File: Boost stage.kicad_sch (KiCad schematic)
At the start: 1 part, among them U49 INA2227AIYBJR

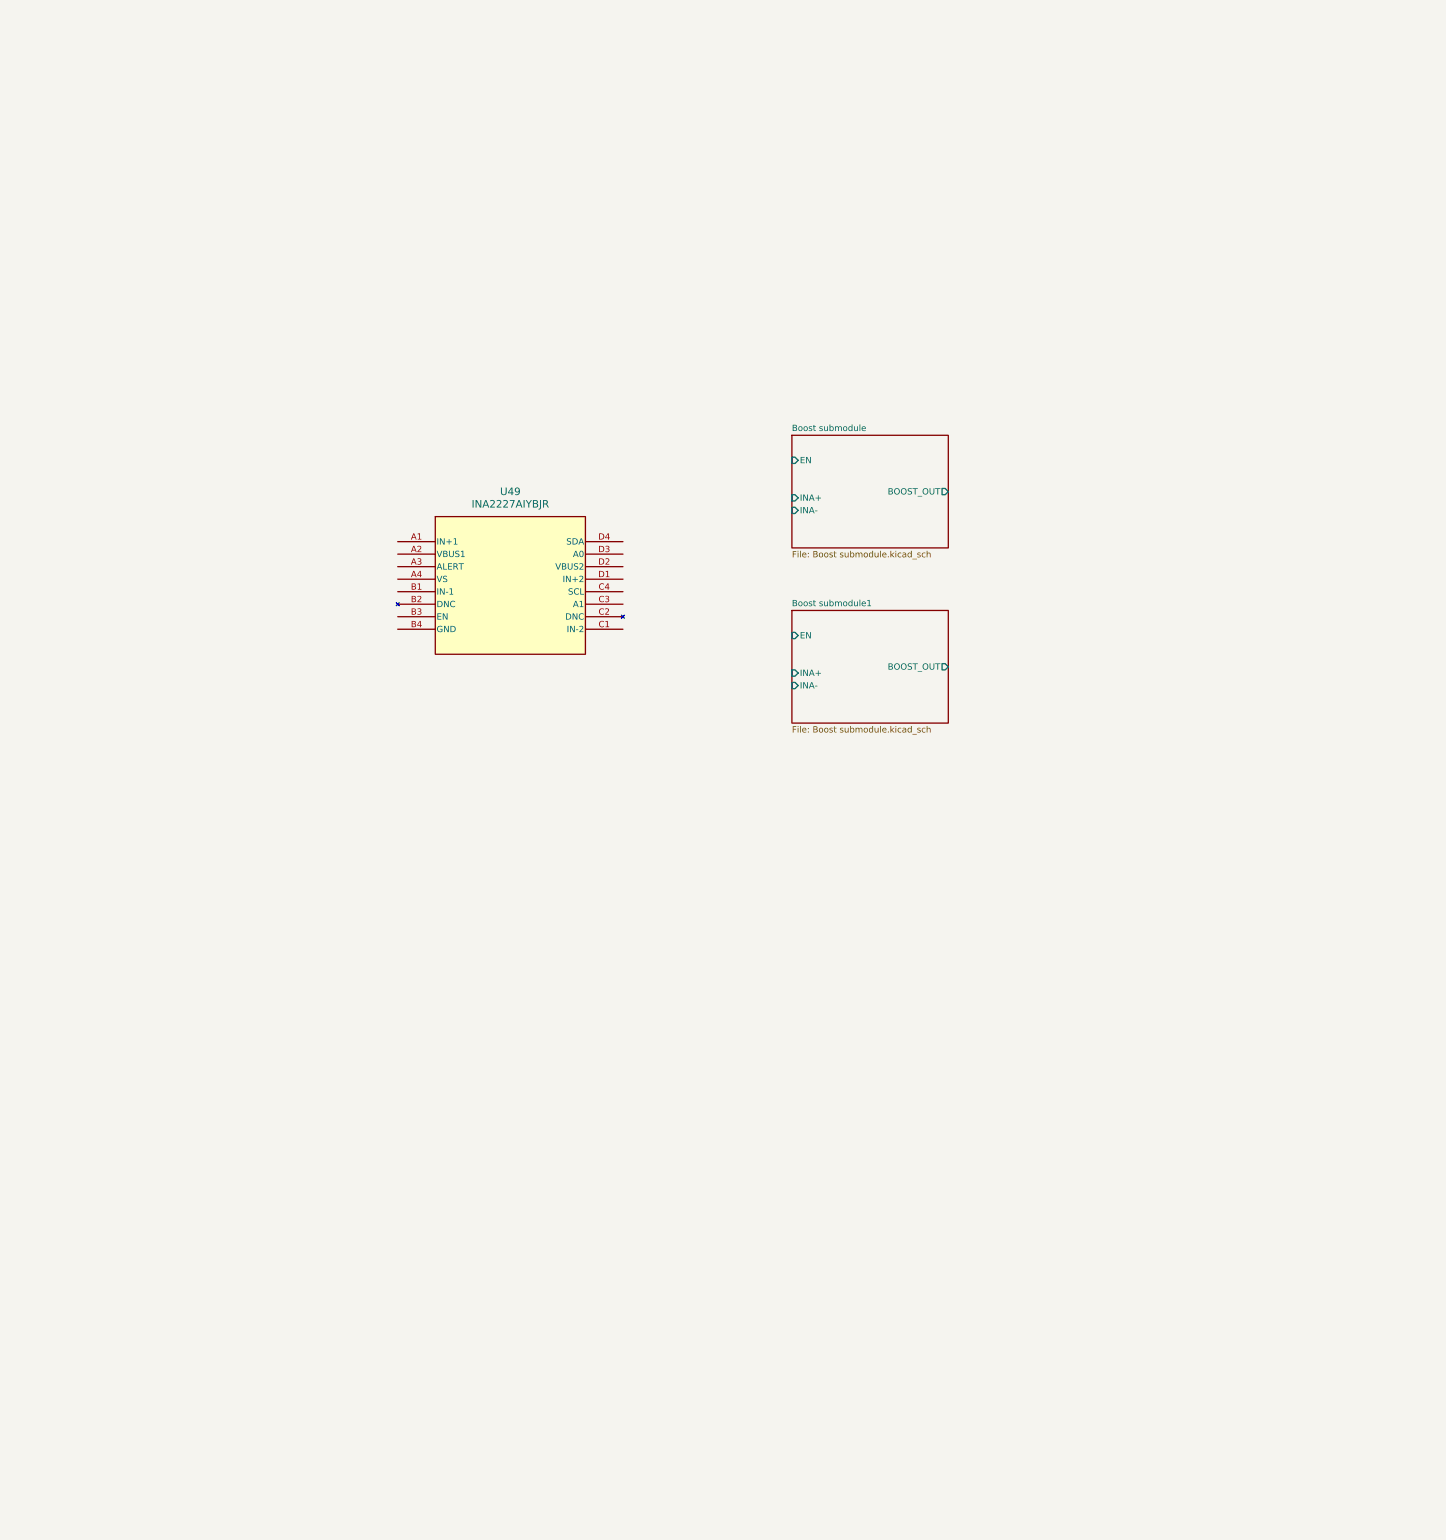
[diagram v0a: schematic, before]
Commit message: HW-61 chore: FT4233 Wire'd up
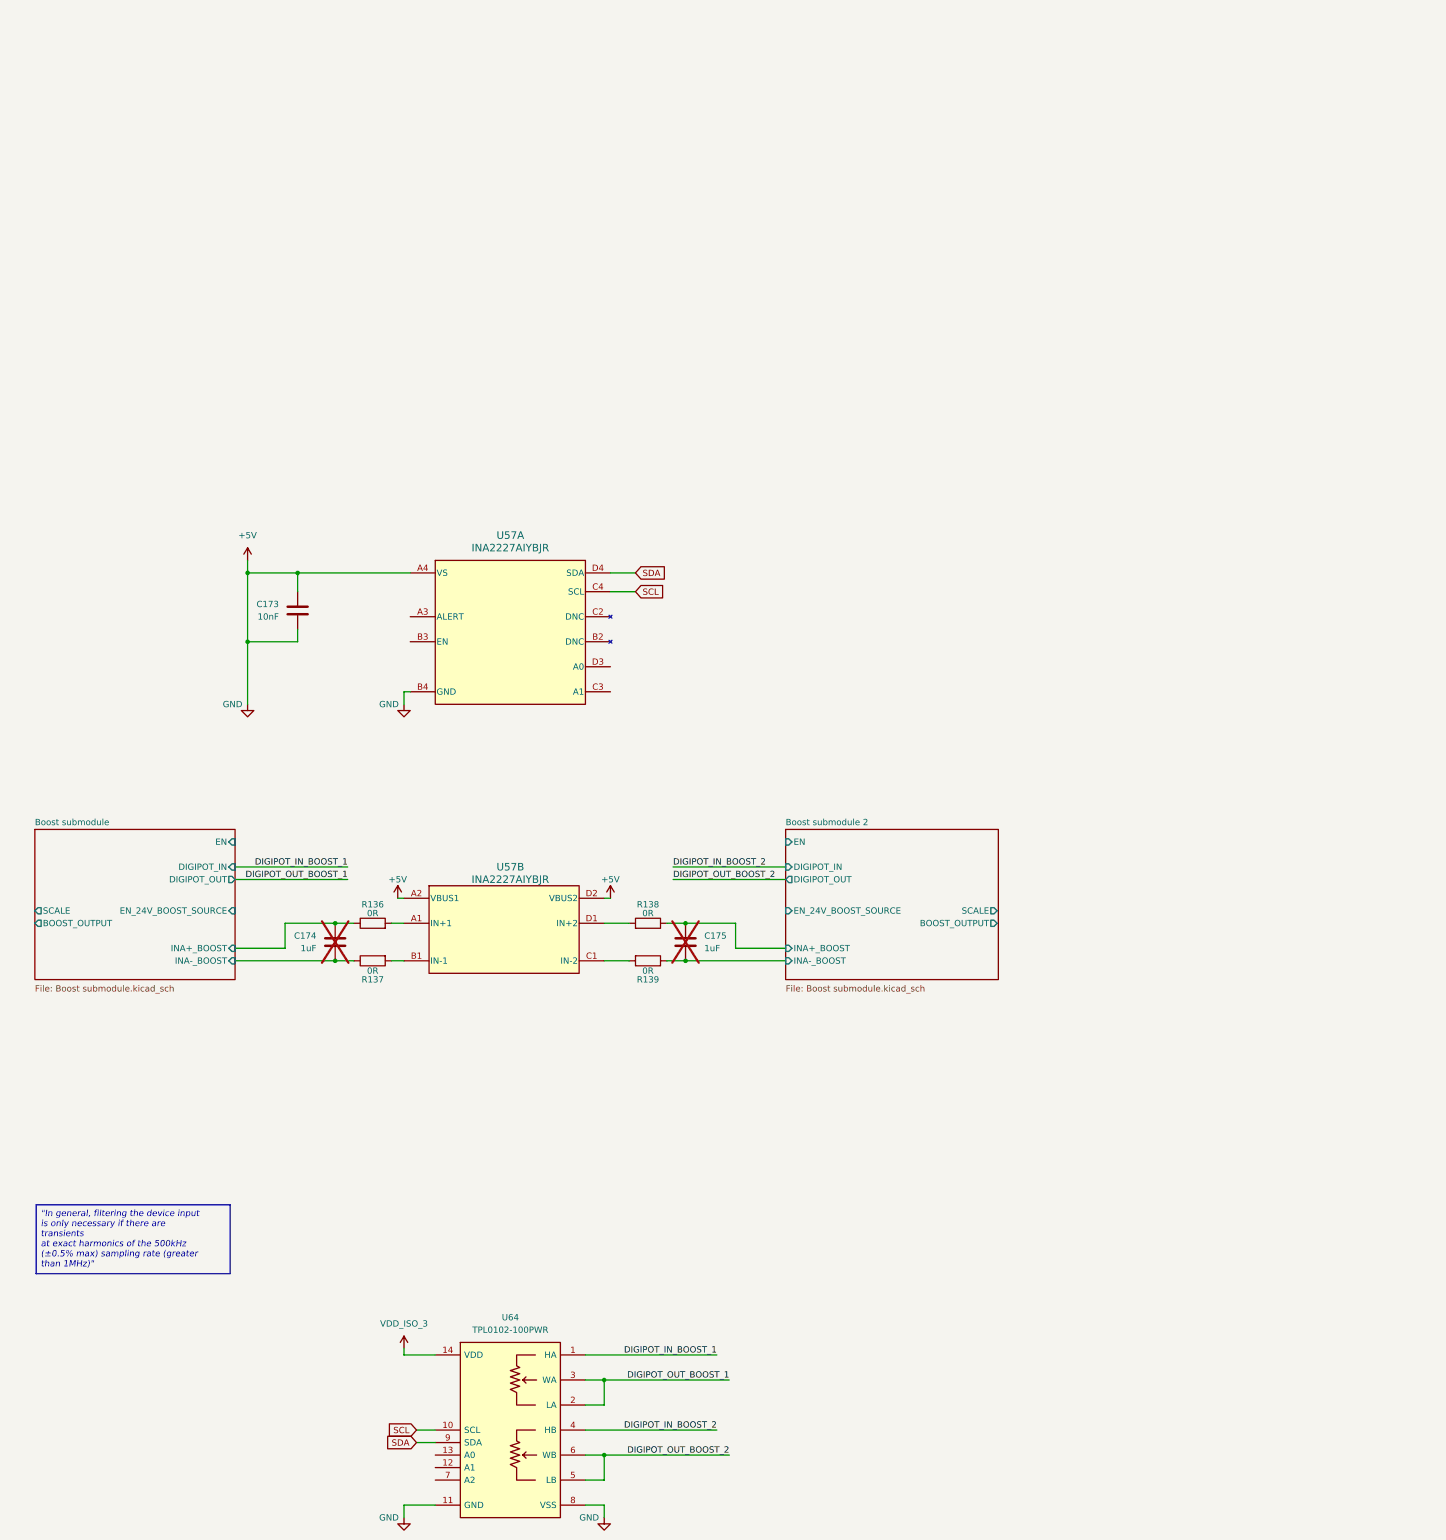
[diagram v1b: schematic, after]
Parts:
- removed U49: INA2227AIYBJR, digikey:U_BGA_YBJ0016-C01_TEX-M, symbol digikey:INA2227AIYBJR
- added C173: 10nF-0402_01, passive:Capacitor_0402, symbol capacitor:10nF-0402_01
- added C174, C175: 1uF-0402_01, passive:Capacitor_0402, symbol capacitor:1uF-0402_01
- added R136, R137, R138, R139: 0R-0402_01, passive:Resistor_0402, symbol resistor:0R-0402_01
- added U57: INA2227AIYBJR, review:DSBGA-16_P0.4_1.508X1.508mm, symbol staging:INA2227AIYBJR
- added U64: TPL0102-100PWR, semiconductor:TSSOP-14_P0.65_4.4x5x1.2, symbol integrated-circuit:TPL0102-100PWR
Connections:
- new net: R139.2, U57.C1 (IN-2)
- new net: R136.2, U57.A1 (IN+1)
- new net: R137.2, U57.B1 (IN-1)
- new net: R138.2, U57.D1 (IN+2)
- new net +5V: C173.1, C173.2, U57.A2 (VBUS1), U57.A4 (VS), U57.B4 (GND), U57.D2 (VBUS2), U64.11 (GND), U64.8 (VSS)
- new net Boost submodule 2/INA+_BOOST: C175.1, R138.1
- new net Boost submodule 2/INA-_BOOST: C175.2, R139.1
- new net Boost submodule/INA+_BOOST: C174.1, R136.1
- new net Boost submodule/INA-_BOOST: C174.2, R137.1
- new net DIGIPOT_IN_BOOST_1: U64.1 (HA)
- new net DIGIPOT_IN_BOOST_2: U64.4 (HB)
- new net DIGIPOT_OUT_BOOST_1: U64.2 (LA), U64.3 (WA)
- new net DIGIPOT_OUT_BOOST_2: U64.5 (LB), U64.6 (WB)
- new net SCL: U57.C4 (SCL), U64.10 (SCL)
- new net SDA: U57.D4 (SDA), U64.9 (SDA)
- new net VDD_ISO_3: U64.14 (VDD)
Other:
- removed sheet Boost submodule1
- added sheet Boost submodule 2 (Boost submodule.kicad_sch)
- sheet Boost submodule ports: added BOOST_OUTPUT, DIGIPOT_IN, DIGIPOT_OUT, EN_24V_BOOST_SOURCE, INA+_BOOST, INA-_BOOST, SCALE; removed BOOST_OUT, INA+, INA-

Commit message: Details to finish
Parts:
- added U68: PCA9535PWR, semiconductor:TSSOP-24_P0.65_7.8x4.4x1.2, symbol integrated-circuit:PCA9535PWR
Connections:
- net +5V: now also U57.B3 (EN), U57.D3 (A0), U68.12 (GND), U68.24 (VDD)
- net SCL: now also U68.22 (SCL)
- net SDA: now also U57.C3 (A1), U68.23 (SDA)
- net Boost submodule 2/INA+_BOOST renamed +INA_BOOST_2
- net Boost submodule 2/INA-_BOOST renamed -INA_BOOST_2
- net Boost submodule/INA+_BOOST renamed +INA_BOOST_1
- net Boost submodule/INA-_BOOST renamed -INA_BOOST_1
- new net EN_BOOST_1: U68.4 (P00_B)
- new net EN_BOOST_2: U68.7 (P03_B)
- new net FEED_24V_BOOST_1: U68.6 (P02_B)
- new net FEED_24V_BOOST_2: U68.9 (P05_B)
- new net FEED_5V_BOOST_1: U68.5 (P01_B)
- new net FEED_5V_BOOST_2: U68.8 (P04_B)
- new net SCALE_BOOST_1: U68.10 (P06_B)
- new net SCALE_BOOST_2: U68.11 (P07_B)
- no-connect marks 0 -> 2
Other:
- sheet Boost submodule ports: added EN_5V_BOOST_SOURCE, EN_BOOST; removed EN
- sheet Boost submodule 2 ports: added EN_5V_BOOST_SOURCE, EN_BOOST; removed EN
- note added: "I2C ID: 0x49"
- moved on the sheet: C173, C174, C175, R136, R137, R138, R139, U57A, U57B, U64

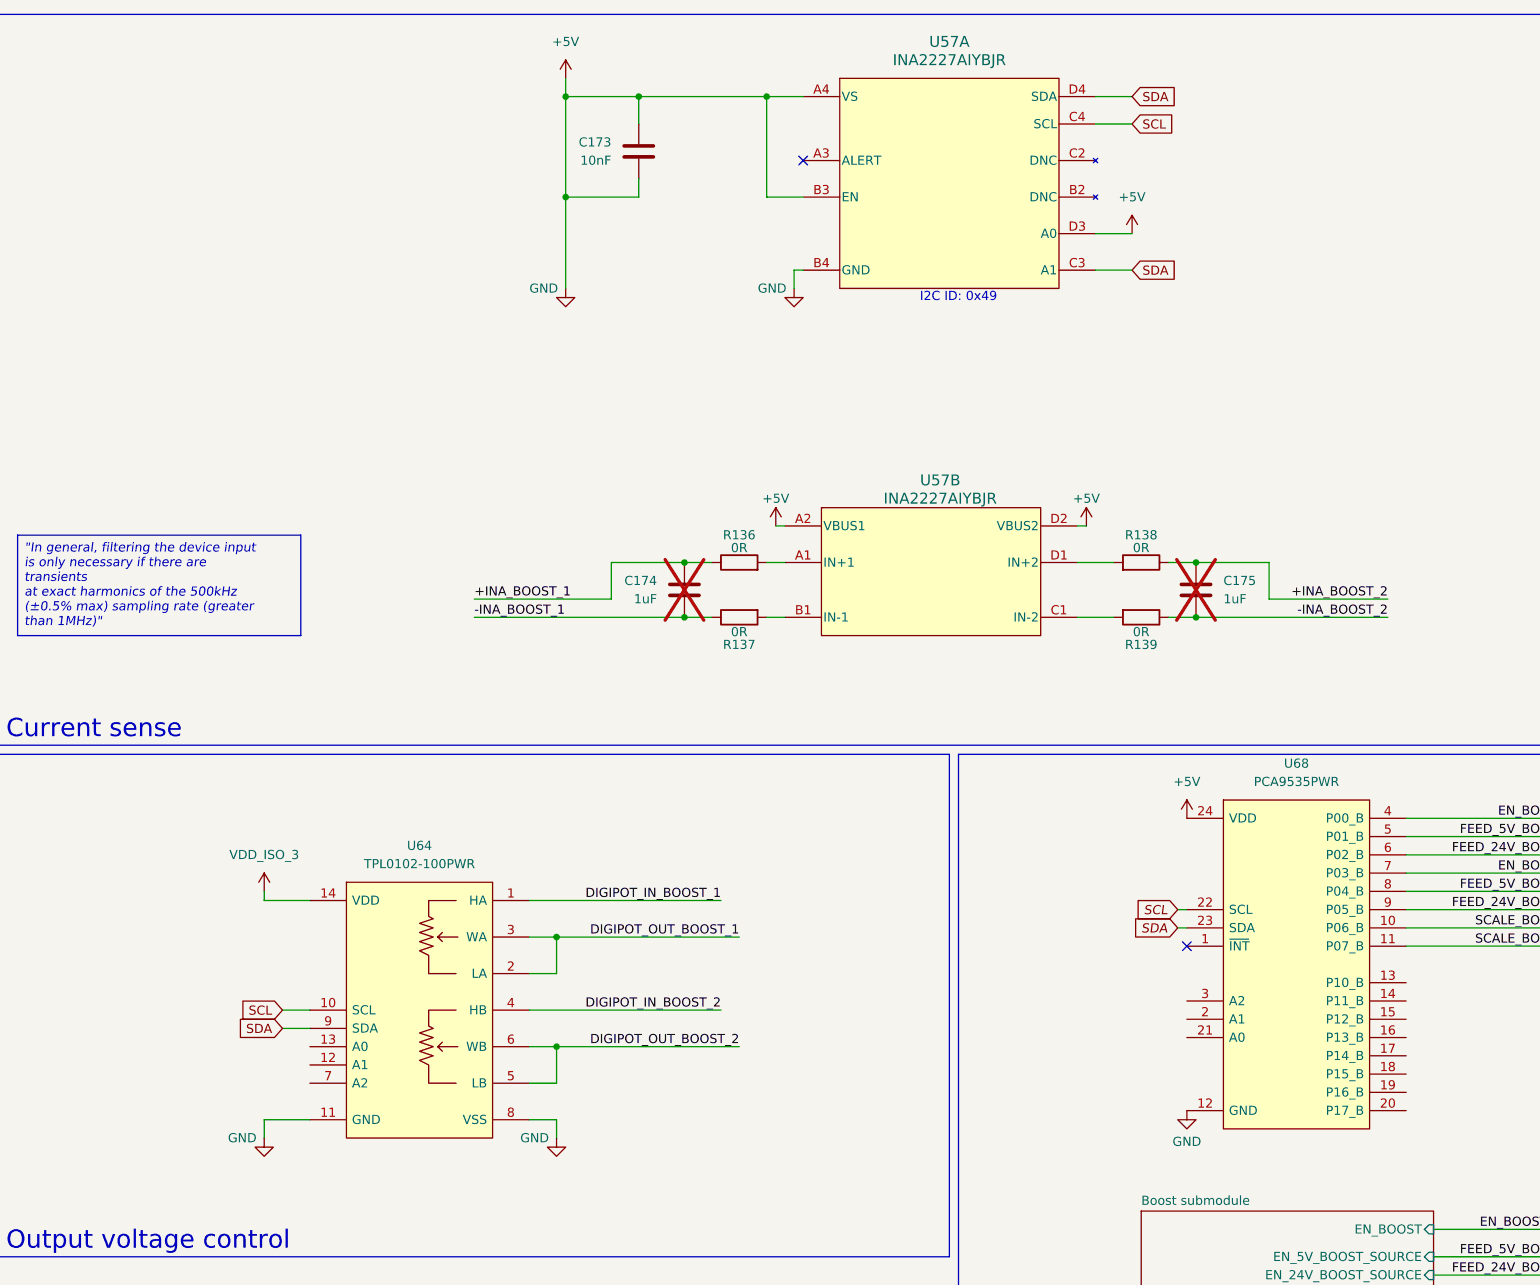
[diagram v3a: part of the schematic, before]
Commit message: HW-61/chore: Added simulation for switch ocntrol, organized the overall schematic, fixed the ERC errors. Still pending for the current sense components and negative side LDO control
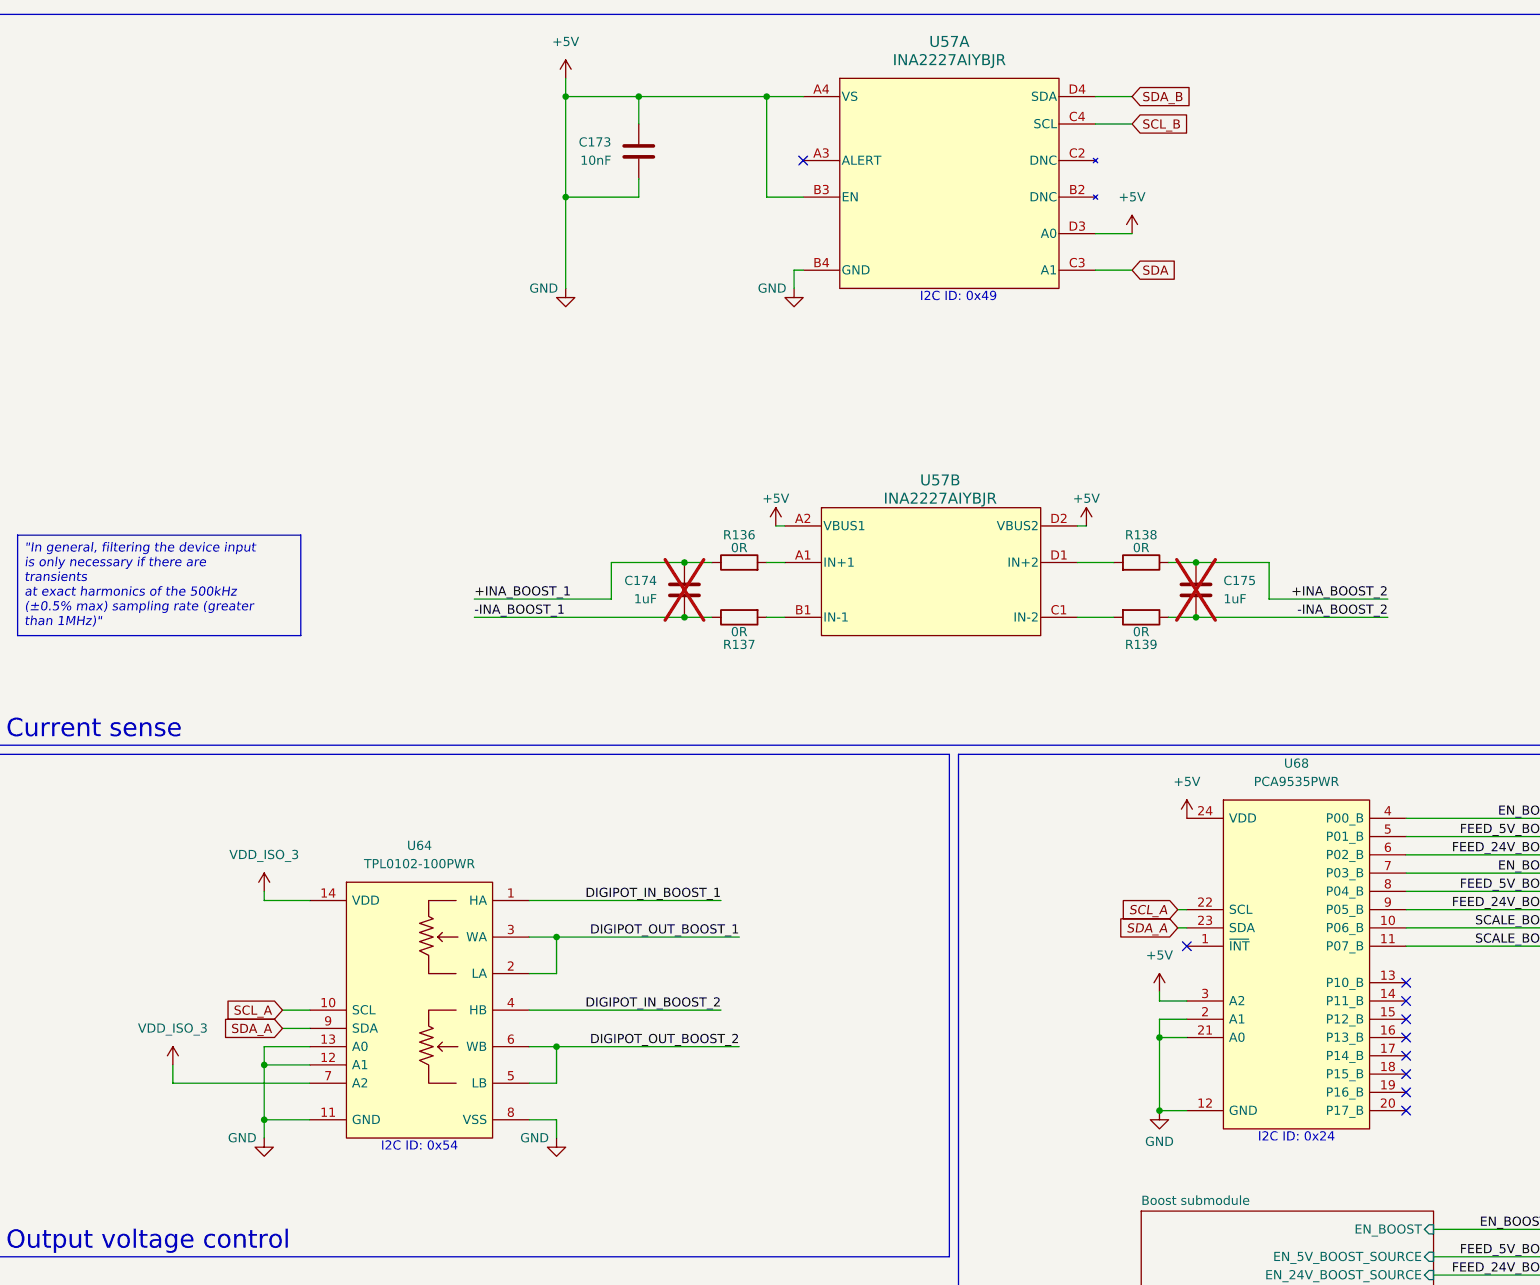
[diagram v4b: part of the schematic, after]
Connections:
- net +5V: now also U64.12 (A1), U64.13 (A0), U68.2 (A1), U68.21 (A0), U68.3 (A2)
- net SDA: no longer U57.D4 (SDA), U64.9 (SDA), U68.23 (SDA)
- net VDD_ISO_3: now also U64.7 (A2)
- net SCL renamed SCL_A
- net SCL_A: no longer U57.C4 (SCL)
- new net SCL_B: U57.C4 (SCL)
- new net SDA_A: U64.9 (SDA), U68.23 (SDA)
- new net SDA_B: U57.D4 (SDA)
- no-connect marks 2 -> 10
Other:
- note added: "I2C ID: 0x24"
- note added: "I2C ID: 0x54"
